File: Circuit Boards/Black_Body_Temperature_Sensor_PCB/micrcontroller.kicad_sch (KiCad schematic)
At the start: 24 parts, among them J2 USB_C_Receptacle_USB2.0_14P, P1 pogo programmer, SW1 430471035826, SW2 430471035826, U4 STM32G431CBTx, Y1 Crystal_GND23

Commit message: Schematic ready for review
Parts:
- removed U4: STM32G431CBTx, Package_QFP:LQFP-48_7x7mm_P0.5mm, symbol MCU_ST_STM32G4:STM32G431CBTx
- added C29: 0.1uf, symbol Device:C
- added C4, C5: C, symbol Device:C
- added D2: D, symbol Device:D
- added J5: Conn_01x06_Pin, symbol Connector:Conn_01x06_Pin
- added U10, U9: STM32G431RBTx, Package_QFP:LQFP-64_10x10mm_P0.5mm, symbol MCU_ST_STM32G4:STM32G431RBTx
- added U11: USBLC6-2SC6, Package_TO_SOT_SMD:SOT-23-6, symbol Power_Protection:USBLC6-2SC6
- added U4: TXU0304, Package_SO:TSSOP-14_4.4x5mm_P0.65mm, symbol -logic_level_shifter:TXU0304
- added U5: AMS1117-3.3, Package_TO_SOT_SMD:SOT-223-3_TabPin2, symbol Regulator_Linear:AMS1117-3.3
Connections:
- net +3V3: now also C29.1, C4.1, U10.1 (VBAT), U10.16 (VDD), U10.32 (VDD), U10.48 (VDD), U10.64 (VDD), U4.1 (VccA), U5.2 (VO)
- net +3V3A: now also U10.28 (VREF+), U10.29 (VDDA)
- net BOOT0: now also U10.61 (PB8)
- net GNDPWR: now also C29.2, C4.2, C5.2, J5.6 (Pin_6), U10.15 (VSS), U10.27 (VSSA), U10.31 (VSS), U10.47 (VSS), U10.63 (VSS), U11.2 (GND), U4.7 (GND), U5.1 (GND)
- net NRST: now also U10.7 (PG10)
- net USB+: now also U10.46 (PA12), U11.4 (I/O2); no longer J2.A6 (D+), J2.B6 (D+)
- net USB-: now also U10.45 (PA11), U11.6 (I/O1); no longer J2.A7 (D-), J2.B7 (D-)
- net XTAL0: now also U10.5 (PF0)
- net XTAL1: now also U10.6 (PF1)
- net hbridge_sel1: now also U10.24 (PB0)
- net hbridge_sel2: now also U10.25 (PB1)
- net hbridge_sel3: now also U10.26 (PB2)
- net hbridge_sel4: now also U10.56 (PB3)
- net i_source_sel1: now also U10.12 (PA0)
- net i_source_sel2: now also U10.13 (PA1), U10.14 (PA2)
- net i_source_sel4: now also U10.17 (PA3)
- net sel.100na_neg: now also U10.57 (PB4)
- net sel.100na_pos: now also U10.58 (PB5)
- net sel.10na_neg: now also U10.59 (PB6)
- net sel.10na_pos: now also U10.60 (PB7)
- net sel_t.100uA: now also U10.19 (PA5)
- net sel_t.10uA: now also U10.20 (PA6)
- net sel_t.1mA: now also U10.18 (PA4)
- net sel_t.1uA: now also U10.21 (PA7)
- net sel_v.100uA: now also U10.43 (PA9)
- net sel_v.10uA: now also U10.44 (PA10)
- net sel_v.1mA: now also U10.42 (PA8)
- net sel_v.1uA: now also U10.51 (PA15)
- net swclk: now also U10.50 (PA14)
- net swdio: now also U10.49 (PA13)
- net at J2.A4 (VBUS), J2.A9 (VBUS), J2.B4 (VBUS)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: now also D2.2 (A)
- new net: U4.6 (NC), U4.9 (NC)
- new net: U9.15 (VSS), U9.31 (VSS), U9.47 (VSS), U9.63 (VSS)
- new net 5Vin: C5.1, D2.1 (K), J5.1 (Pin_1), U11.5 (VBUS), U4.14 (VccB), U5.3 (VI)
- new net CLK: U4.3 (A2)
- new net CLK_5V: J5.3 (Pin_3), U4.12 (B2Y)
- new net CS: U4.4 (A3)
- new net CS_5V: J5.4 (Pin_4), U4.11 (B3Y)
- new net MISO: U4.5 (A4Y)
- new net MISO_5V: J5.5 (Pin_5), U4.10 (B4)
- new net MOSI: U4.2 (A1)
- new net MOSI_5V: J5.2 (Pin_2), U4.13 (B1Y)
- new net OE: U4.8 (OE)
- new net USB_RAW+: J2.A6 (D+), J2.B6 (D+), U11.3 (I/O2)
- new net USB_RAW-: J2.A7 (D-), J2.B7 (D-), U11.1 (I/O1)
- new net i_sense_sel1: U10.34 (PB12)
- new net i_sense_sel2: U10.35 (PB13)
- new net i_sense_sel3: U10.36 (PB14)
- new net i_sense_sel4: U10.37 (PB15)
- no-connect marks 12 -> 21
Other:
- note added: "Level shifted SPI"
- note added: "Microcontroller 3.3V"
- note added: "USB-C"
- note removed: "USB-C w/o power"
- moved on the sheet: C13, C16, C17, J2, P1, R18, R20, R21, SW2

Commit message: Temperature Sensor Schematic Done, awaiting review
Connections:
- net OE is gone; now on net +3V3: U4.8 (OE)
- net CLK: now also U10.52 (PC10)
- net MISO: now also U10.53 (PC11)
- net MOSI: now also U10.54 (PC12)
- net USB+: no longer U11.4 (I/O2)
- net USB-: no longer U11.6 (I/O1)
- net hbridge_sel1: now also U10.56 (PB3); no longer U10.24 (PB0)
- net hbridge_sel2: now also U10.57 (PB4); no longer U10.25 (PB1)
- net hbridge_sel3: now also U10.58 (PB5); no longer U10.26 (PB2)
- net hbridge_sel4: now also U10.59 (PB6); no longer U10.56 (PB3)
- net i_sense_sel1: now also U10.8 (PC0); no longer U10.34 (PB12)
- net i_sense_sel2: now also U10.9 (PC1); no longer U10.35 (PB13)
- net i_sense_sel3: now also U10.10 (PC2); no longer U10.36 (PB14)
- net i_sense_sel4: now also U10.11 (PC3); no longer U10.37 (PB15)
- net sel.100na_neg: now also U10.60 (PB7); no longer U10.57 (PB4)
- net sel.100na_pos: now also U10.62 (PB9); no longer U10.58 (PB5)
- net sel.10na_neg: now also U10.30 (PB10); no longer U10.59 (PB6)
- net sel.10na_pos: now also U10.33 (PB11); no longer U10.60 (PB7)
- net sel_v.100uA: now also U10.44 (PA10); no longer U10.43 (PA9)
- net sel_v.10uA: now also U10.24 (PB0); no longer U10.44 (PA10)
- net sel_v.1mA: now also U10.43 (PA9); no longer U10.42 (PA8)
- net sel_v.1uA: now also U10.25 (PB1); no longer U10.51 (PA15)
- net VBUS: now reaches D2.2 (A), J2.A4 (VBUS), J2.A9 (VBUS), J2.B4 (VBUS), J2.B9 (VBUS)
- net CC1: now reaches J2.A5 (CC1), R21.1
- net ADC_DRDY: now reaches U10.39 (PC7)
- net CC2: now reaches J2.B5 (CC2), R20.2
- net +3V3A renamed +3V3d
- net CS renamed shft_CS
- net shft_CS: now also U10.51 (PA15)
- new net CLK_MCO: U10.42 (PA8)
- new net SPI.CS: U10.34 (PB12)
- new net SPI.MISO: U10.36 (PB14)
- new net SPI.MOSI: U10.37 (PB15)
- new net SPI.SCLK: U10.35 (PB13)
- no-connect marks 21 -> 1
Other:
- moved on the sheet: D2, R20, R21

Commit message: Temp sensor schematic done
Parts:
- removed C4, C5: C, symbol Device:C
- removed D2: D, symbol Device:D
- removed J2: USB_C_Receptacle_USB2.0_14P, symbol Connector:USB_C_Receptacle_USB2.0_14P
- removed J5: Conn_01x06_Pin, symbol Connector:Conn_01x06_Pin
- removed SW1, SW2: 430471035826, -switch:430471035826, symbol -switch:SW_Push
- removed U5: AMS1117-3.3, Package_TO_SOT_SMD:SOT-223-3_TabPin2, symbol Regulator_Linear:AMS1117-3.3
- removed Y1: Crystal_GND23, symbol Device:Crystal_GND23
- added C713: 10uf, Capacitor_SMD:C_0603_1608Metric, symbol Device:C
- added C716: 22uf, Capacitor_SMD:C_0603_1608Metric, symbol Device:C
- added D701: 1N5819WS, Diode_SMD:D_SOD-323, symbol Diode:1N5819WS
- added J701: Conn_01x06_Pin, Connector_PinHeader_2.54mm:PinHeader_1x06_P2.54mm_Vertical, symbol Connector:Conn_01x06_Pin
- added J702: USB_C_Receptacle_USB2.0_16P, -connector:UJ20-C-H-G-SMT-1-P16-TR, symbol Connector:USB_C_Receptacle_USB2.0_16P
- added J703: 5040500891, -connector:CONN_5040500891_MOL, symbol -connector:5040500891
- added SW701, SW702: SW_MEC_5E, -switch:430471035826, symbol Switch:SW_MEC_5E
- added U704: AMS1117-3.3, Package_TO_SOT_SMD:SOT-223-3_TabPin2, symbol Regulator_Linear:AMS1117-3.3
- added U706: ABM8G-25.000MHZ-18-D2Y-T, -oscillators:ABM8G-25.000MHZ-18-D2Y-T, symbol -oscillator:ABM8G-25.000MHZ-18-D2Y-T
- C701: renamed from C12; footprint (none) -> Capacitor_SMD:C_0603_1608Metric
- C702: renamed from C8; footprint (none) -> Capacitor_SMD:C_0603_1608Metric
- C703: renamed from C3; value pf -> 28pf; footprint (none) -> Capacitor_SMD:C_0603_1608Metric
- C704: renamed from C17; footprint (none) -> Capacitor_SMD:C_0603_1608Metric
- C705: renamed from C9; footprint (none) -> Capacitor_SMD:C_0603_1608Metric
- C706: renamed from C2; value pf -> 28pf; footprint (none) -> Capacitor_SMD:C_0603_1608Metric
- C707: renamed from C16; footprint (none) -> Capacitor_SMD:C_0603_1608Metric
- C708: renamed from C10; footprint (none) -> Capacitor_SMD:C_0603_1608Metric
- C709: renamed from C11; footprint (none) -> Capacitor_SMD:C_0603_1608Metric
- C710: renamed from C29; footprint (none) -> Capacitor_SMD:C_0603_1608Metric
- C711: renamed from C14; footprint (none) -> Capacitor_SMD:C_0603_1608Metric
- C712: renamed from C15; footprint (none) -> Capacitor_SMD:C_0603_1608Metric
- C714: renamed from C7; footprint (none) -> Capacitor_SMD:C_0603_1608Metric
- C715: renamed from C13; footprint (none) -> Capacitor_SMD:C_0603_1608Metric
- FB701: renamed from FB1; value FerriteBead -> BLM18AG102SN1D; footprint (none) -> Inductor_SMD:L_0201_0603Metric
- R701: renamed from R21; footprint (none) -> Resistor_SMD:R_0603_1608Metric
- R702: renamed from R20; footprint (none) -> Resistor_SMD:R_0603_1608Metric
- R703: renamed from R19; footprint (none) -> Resistor_SMD:R_0603_1608Metric
- R704: renamed from R18; footprint (none) -> Resistor_SMD:R_0603_1608Metric
- renumbered P1 to P701, U4 to U701, U11 to U702, U10 to U703, U9 to U705
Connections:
- net +3V3: now also C716.1, U704.2 (VO)
- net 5Vin: now also D701.1 (K), J701.1 (Pin_1), J703.1
- net BOOT0: now also SW702.2
- net CC1: now also J702.A5 (CC1)
- net CC2: now also J702.B5 (CC2)
- net CLK: now also U701.4 (A3); no longer U701.3 (A2)
- net CLK_5V: now also U701.11 (B3Y), J701.4 (Pin_4), J703.6; no longer U701.12 (B2Y)
- net CS_5V: now also U701.13 (B1Y), J701.2 (Pin_2), J703.4; no longer U701.11 (B3Y)
- net GNDPWR: now also J701.6 (Pin_6), J702.A1 (GND), J702.A12 (GND), J702.B1 (GND), J702.B12 (GND), J703.8, SW701.3 (K), SW702.3 (K), U706.2 (G), U706.4 (G)
- net MISO_5V: now also J701.5 (Pin_5), J703.7
- net MOSI: now also U701.3 (A2); no longer U701.2 (A1)
- net MOSI_5V: now also U701.12 (B2Y), J701.3 (Pin_3), J703.5; no longer U701.13 (B1Y)
- net NRST: now also SW701.2
- net USB+: now also U702.4 (I/O2)
- net USB-: now also U702.6 (I/O1)
- net USB_RAW+: now also J702.A6 (D+), J702.B6 (D+)
- net USB_RAW-: now also J702.A7 (D-), J702.B7 (D-)
- net VBUS: now also D701.2 (A), J702.A4 (VBUS), J702.A9 (VBUS), J702.B4 (VBUS), J702.B9 (VBUS)
- net XTAL0: now also U706.1
- net XTAL1: now also U706.3
- net i_source_sel2: no longer U703.14 (PA2)
- net shft_CS renamed CS
- net CS: now also U701.2 (A1); no longer U701.4 (A3)
- new net +5V: C713.1, U704.3 (VI)
- new net GND: C713.2, C716.2, U704.1 (GND)
- new net i_source_sel3: U703.14 (PA2)
- no-connect marks 1 -> 19
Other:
- note added: "Microcontroller (PAGE 7)"
- moved on the sheet: C701, C702, C703, C704, C705, C706, C707, C708, C709, C710, C711, C712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

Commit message: temp pcb analog layout done
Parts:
- removed C704, C711, C712: 0.1uf, Capacitor_SMD:C_0603_1608Metric, symbol Device:C
- removed FB701: BLM18AG102SN1D, Inductor_SMD:L_0201_0603Metric, symbol Device:FerriteBead
- removed J703: 5040500891, -connector:CONN_5040500891_MOL, symbol -connector:5040500891
- removed U705: STM32G431RBTx, Package_QFP:LQFP-64_10x10mm_P0.5mm, symbol MCU_ST_STM32G4:STM32G431RBTx
- added J702: 5040500891, -connector:CONN_5040500891_MOL, symbol -connector:5040500891
- C701: value 10uf -> 0.1uf
- J701: now not fitted; now left out of the parts list
- P701: now left out of the parts list
- renumbered J702 to J703, U706 to U702, U702 to U703, U703 to U704, U704 to U705
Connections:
- net +3V3d is gone; now on net +3V3: C707.1, U704.28 (VREF+), U704.29 (VDDA)
- net +5V is gone; now on net 5Vin: C713.1, U705.3 (VI)
- net GND is gone; now on net GNDPWR: C713.2, C716.2, U705.1 (GND)
- net 5Vin: now also J701.6 (Pin_6), J702.8; no longer J701.1 (Pin_1)
- net CLK_5V: now also J701.3 (Pin_3), J702.3; no longer J701.4 (Pin_4)
- net CS_5V: now also J701.5 (Pin_5), J702.5; no longer J701.2 (Pin_2)
- net GNDPWR: now also J701.1 (Pin_1), J702.1; no longer J701.6 (Pin_6)
- net MISO_5V: now also J701.2 (Pin_2), J702.2; no longer J701.5 (Pin_5)
- net MOSI_5V: now also J701.4 (Pin_4), J702.4; no longer J701.3 (Pin_3)
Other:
- moved on the sheet: C707

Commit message: Digital section done
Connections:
- net ADC_DRDY: now also U704.8 (PC0); no longer U704.39 (PC7)
- net CLK: now also U704.35 (PB13); no longer U704.52 (PC10)
- net CS: now also U704.34 (PB12); no longer U704.51 (PA15)
- net MISO: now also U704.36 (PB14); no longer U704.53 (PC11)
- net MOSI: now also U704.37 (PB15); no longer U704.54 (PC12)
- net SPI.CS: now also U704.51 (PA15); no longer U704.34 (PB12)
- net SPI.MISO: now also U704.53 (PC11); no longer U704.36 (PB14)
- net SPI.MOSI: now also U704.54 (PC12); no longer U704.37 (PB15)
- net SPI.SCLK: now also U704.52 (PC10); no longer U704.35 (PB13)
- net i_sense_sel1: now also U704.9 (PC1); no longer U704.8 (PC0)
- net i_sense_sel2: now also U704.10 (PC2); no longer U704.9 (PC1)
- net i_sense_sel3: now also U704.11 (PC3); no longer U704.10 (PC2)
- net i_sense_sel4: now also U704.22 (PC4); no longer U704.11 (PC3)
- no-connect marks 19 -> 18

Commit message: Complete except for recommended changes
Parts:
- R701, R702: footprint Resistor_SMD:R_0603_1608Metric -> Resistor_SMD:R_0402_1005Metric
- renumbered C705 to C704, C706 to C705, C708 to C706, C709 to C708, C710 to C711, C713 to C712, C714 to C713, C715 to C714, C716 to C715, R703 to R704, R704 to R705
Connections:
- net CC1: now also R701.2; no longer R701.1
- net GNDPWR: now also P701.3 (GND), R701.1; no longer P701.4 (GND), R701.2
- net hbridge_sel1: now also U704.19 (PA5); no longer U704.56 (PB3)
- net hbridge_sel2: now also U704.20 (PA6); no longer U704.57 (PB4)
- net hbridge_sel3: now also U704.18 (PA4); no longer U704.58 (PB5)
- net hbridge_sel4: now also U704.14 (PA2); no longer U704.59 (PB6)
- net i_sense_sel1: now also U704.11 (PC3); no longer U704.9 (PC1)
- net i_sense_sel2: now also U704.12 (PA0); no longer U704.10 (PC2)
- net i_sense_sel3: now also U704.13 (PA1); no longer U704.11 (PC3)
- net i_sense_sel4: now also U704.17 (PA3); no longer U704.22 (PC4)
- net i_source_sel1: now also U704.23 (PC5); no longer U704.12 (PA0)
- net i_source_sel2: now also U704.10 (PC2); no longer U704.13 (PA1)
- net i_source_sel3: now also U704.9 (PC1); no longer U704.14 (PA2)
- net i_source_sel4: now also U704.4 (PC15); no longer U704.17 (PA3)
- net sel.100na_neg: now also U704.24 (PB0); no longer U704.60 (PB7)
- net sel.100na_pos: now also U704.22 (PC4); no longer U704.62 (PB9)
- net sel.10na_pos: now also U704.21 (PA7); no longer U704.33 (PB11)
- net sel_t.100uA: now also U704.60 (PB7); no longer U704.19 (PA5)
- net sel_t.10uA: now also U704.62 (PB9); no longer U704.20 (PA6)
- net sel_t.1mA: now also U704.25 (PB1); no longer U704.18 (PA4)
- net sel_t.1uA: now also U704.26 (PB2); no longer U704.21 (PA7)
- net sel_v.100uA: now also U704.57 (PB4); no longer U704.44 (PA10)
- net sel_v.10uA: now also U704.55 (PD2); no longer U704.24 (PB0)
- net sel_v.1mA: now also U704.2 (PC13); no longer U704.43 (PA9)
- net sel_v.1uA: now also U704.58 (PB5); no longer U704.25 (PB1)
- net swclk: now also P701.4 (SWCLK); no longer P701.3 (SWCLK)
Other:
- note added: "Solderable connector"
- moved on the sheet: J701, J702, P701, U701

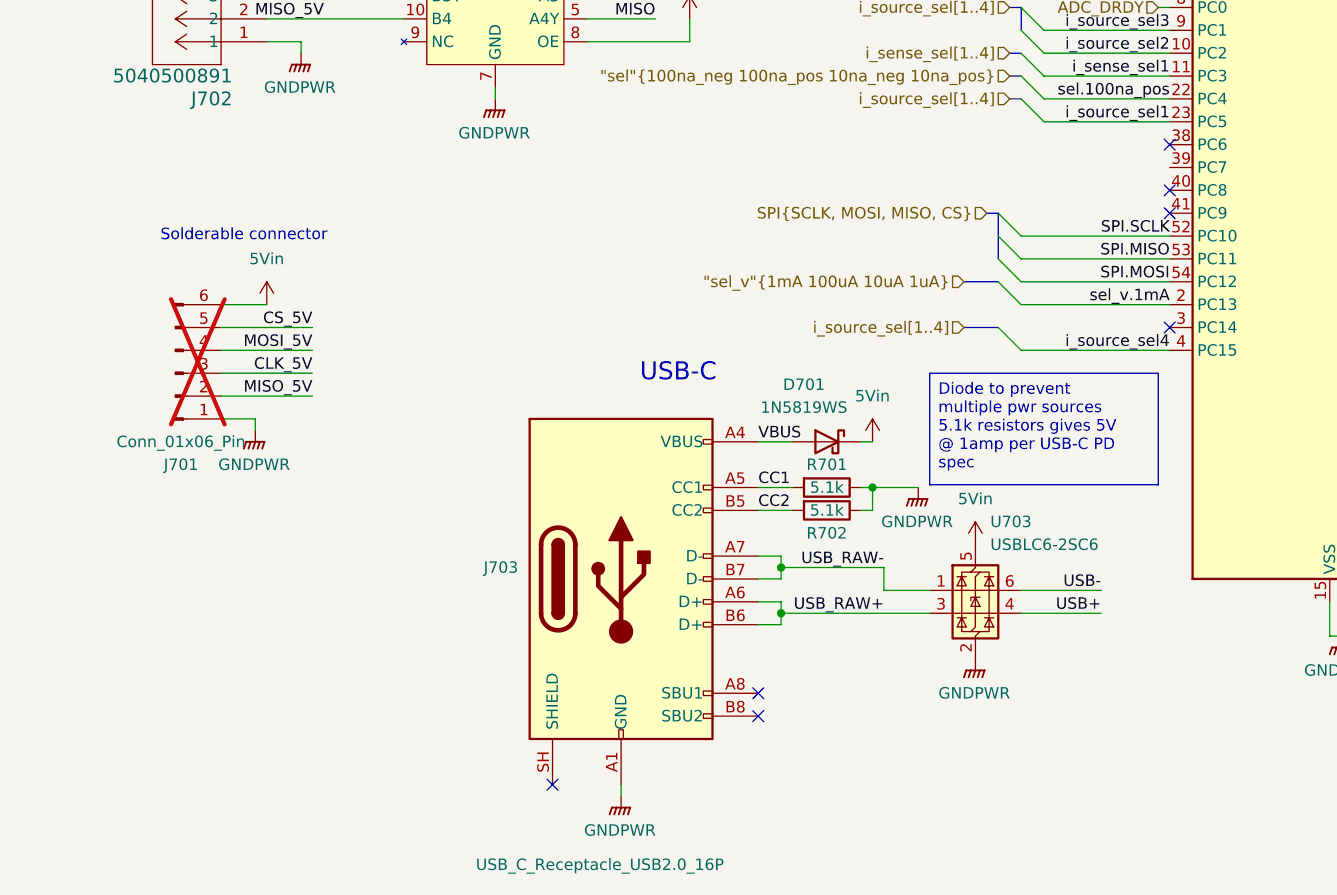
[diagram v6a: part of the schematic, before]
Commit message: Heater switched from pwm to vccs
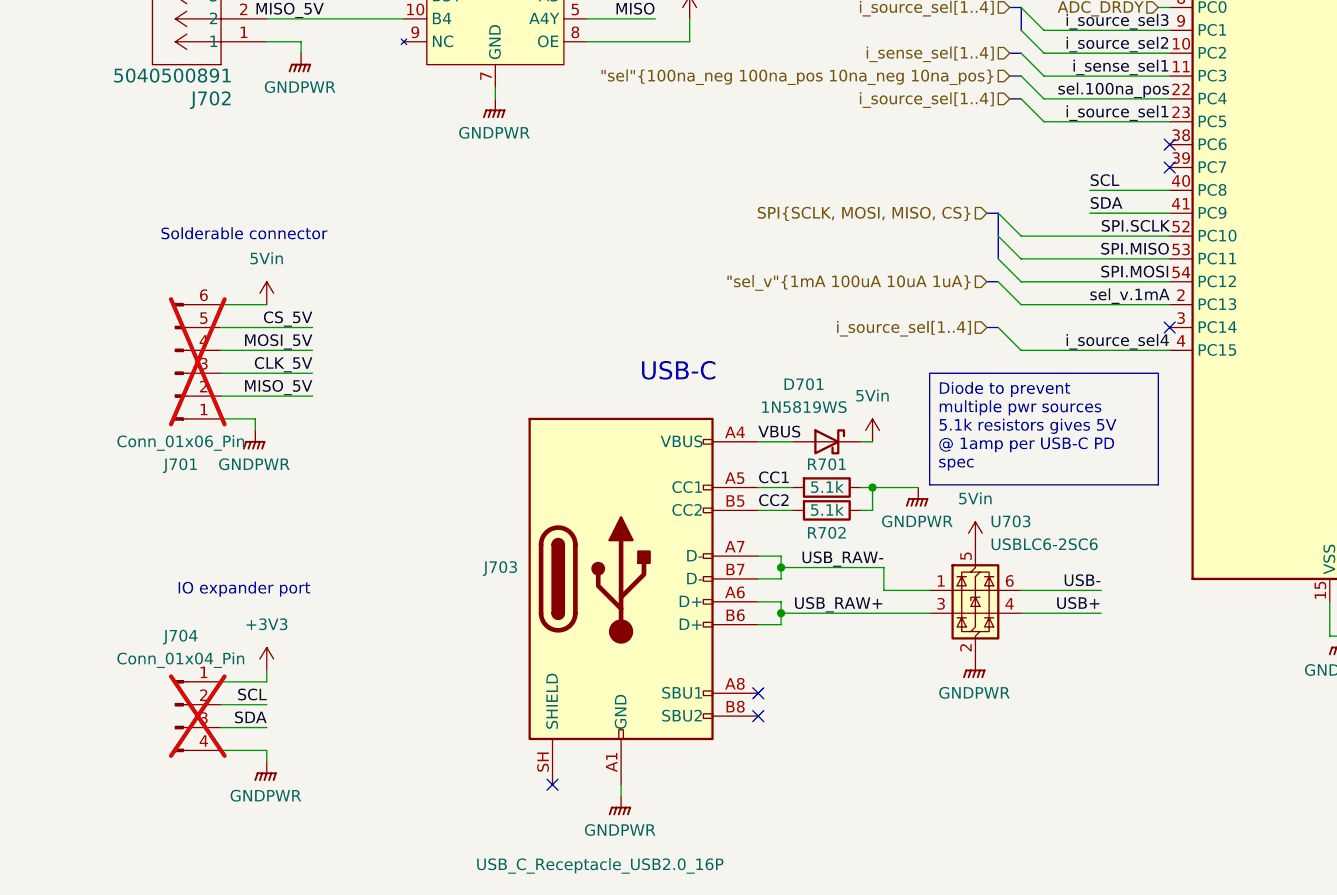
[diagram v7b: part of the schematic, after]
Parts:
- added J704: Conn_01x04_Pin, Connector_PinHeader_2.54mm:PinHeader_1x04_P2.54mm_Vertical, symbol Connector:Conn_01x04_Pin
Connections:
- net +3V3: now also J704.1 (Pin_1)
- net GNDPWR: now also J704.4 (Pin_4)
- net SCL: now reaches U704.40 (PC8)
- net SCL: now also J704.2 (Pin_2)
- net SDA: now reaches U704.41 (PC9)
- net SDA: now also J704.3 (Pin_3)
- no-connect marks 18 -> 17
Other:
- note added: "IO expander port"
